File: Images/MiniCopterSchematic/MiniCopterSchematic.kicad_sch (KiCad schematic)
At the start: 21 parts, among them J1 MPU6050, M1 Motor_DC_1, M2 Motor_DC_2, M3 Motor_DC_3, M4 Motor_DC_4, Q1 FQP20NO6L, Q2 FQP20NO6L, Q3 FQP20NO6L, Q4 FQP20NO6L

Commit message: Working on PCB
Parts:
- added C1: 47UF-CAPACITOR, Capacitor_THT:CP_Radial_D4.0mm_P1.50mm, symbol SparkFun-Capacitors:47UF-POLAR-EIA3528-10V-10%
- added JP1: SolderJumper_1, Connector_PinSocket_2.54mm:PinSocket_1x02_P2.54mm_Vertical, symbol Jumper:SolderJumper_2_Open
- added JP2: SolderJumper_2, Connector_PinSocket_2.54mm:PinSocket_1x02_P2.54mm_Vertical, symbol Jumper:SolderJumper_2_Open
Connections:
- net +5V: now also C1.A (+)
- net GND: now also C1.C (-), JP1.2 (B)
- net at J1.7 (AD0): now also JP1.1 (A)
- net at J1.8 (INT): now also JP2.1 (A)
- net INT: now reaches A1.5 (D2)
- net INT: now also JP2.2 (B)
- no-connect marks 20 -> 17
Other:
- moved on the sheet: J1

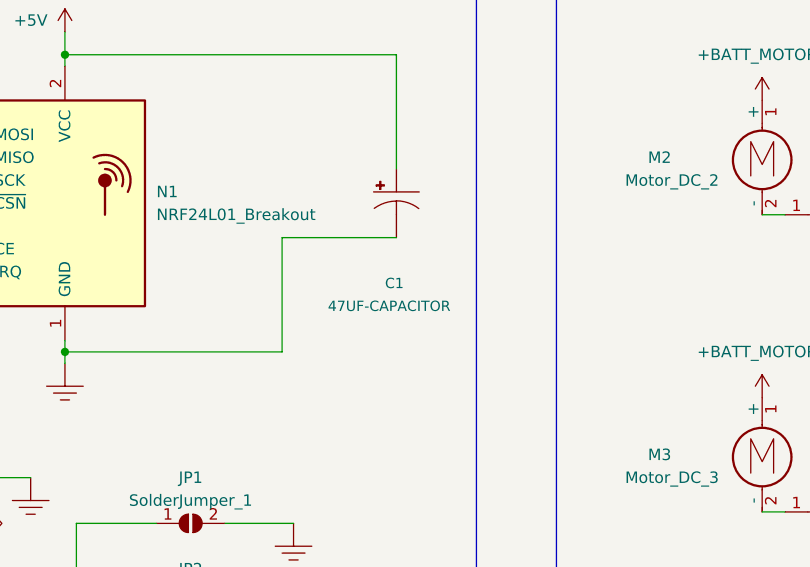
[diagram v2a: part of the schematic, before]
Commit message: Added capacitor, changed track widths on PCB
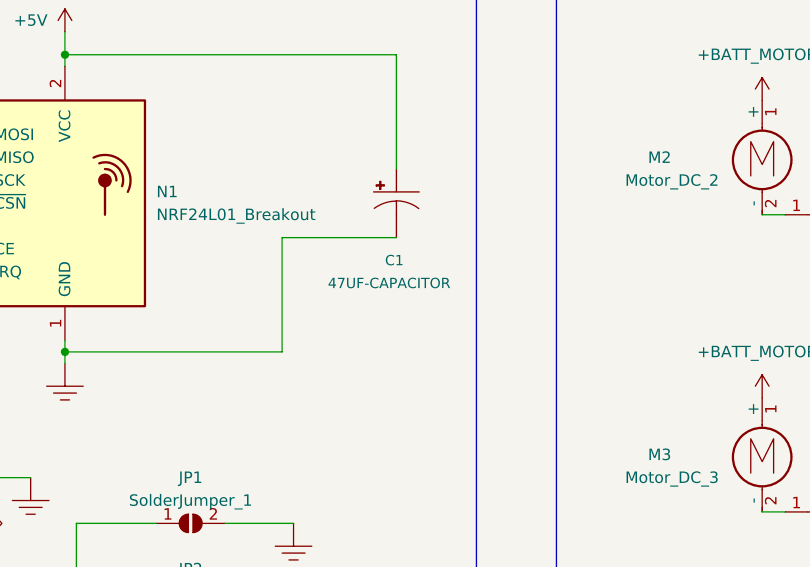
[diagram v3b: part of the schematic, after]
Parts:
- removed C1: 47UF-CAPACITOR, Capacitor_THT:CP_Radial_D4.0mm_P1.50mm, symbol SparkFun-Capacitors:47UF-POLAR-EIA3528-10V-10%
- added C1: 47UF-CAPACITOR, Capacitor_THT:CP_Radial_D6.3mm_P2.50mm, symbol AA_Custom_Components:47UF-CAPACITOR
- JP1, JP2: footprint Connector_PinSocket_2.54mm:PinSocket_1x02_P2.54mm_Vertical -> Connector_PinHeader_2.54mm:PinHeader_1x02_P2.54mm_Vertical
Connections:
- net +5V: now also C1.1 (+)
- net GND: now also C1.2 (-)

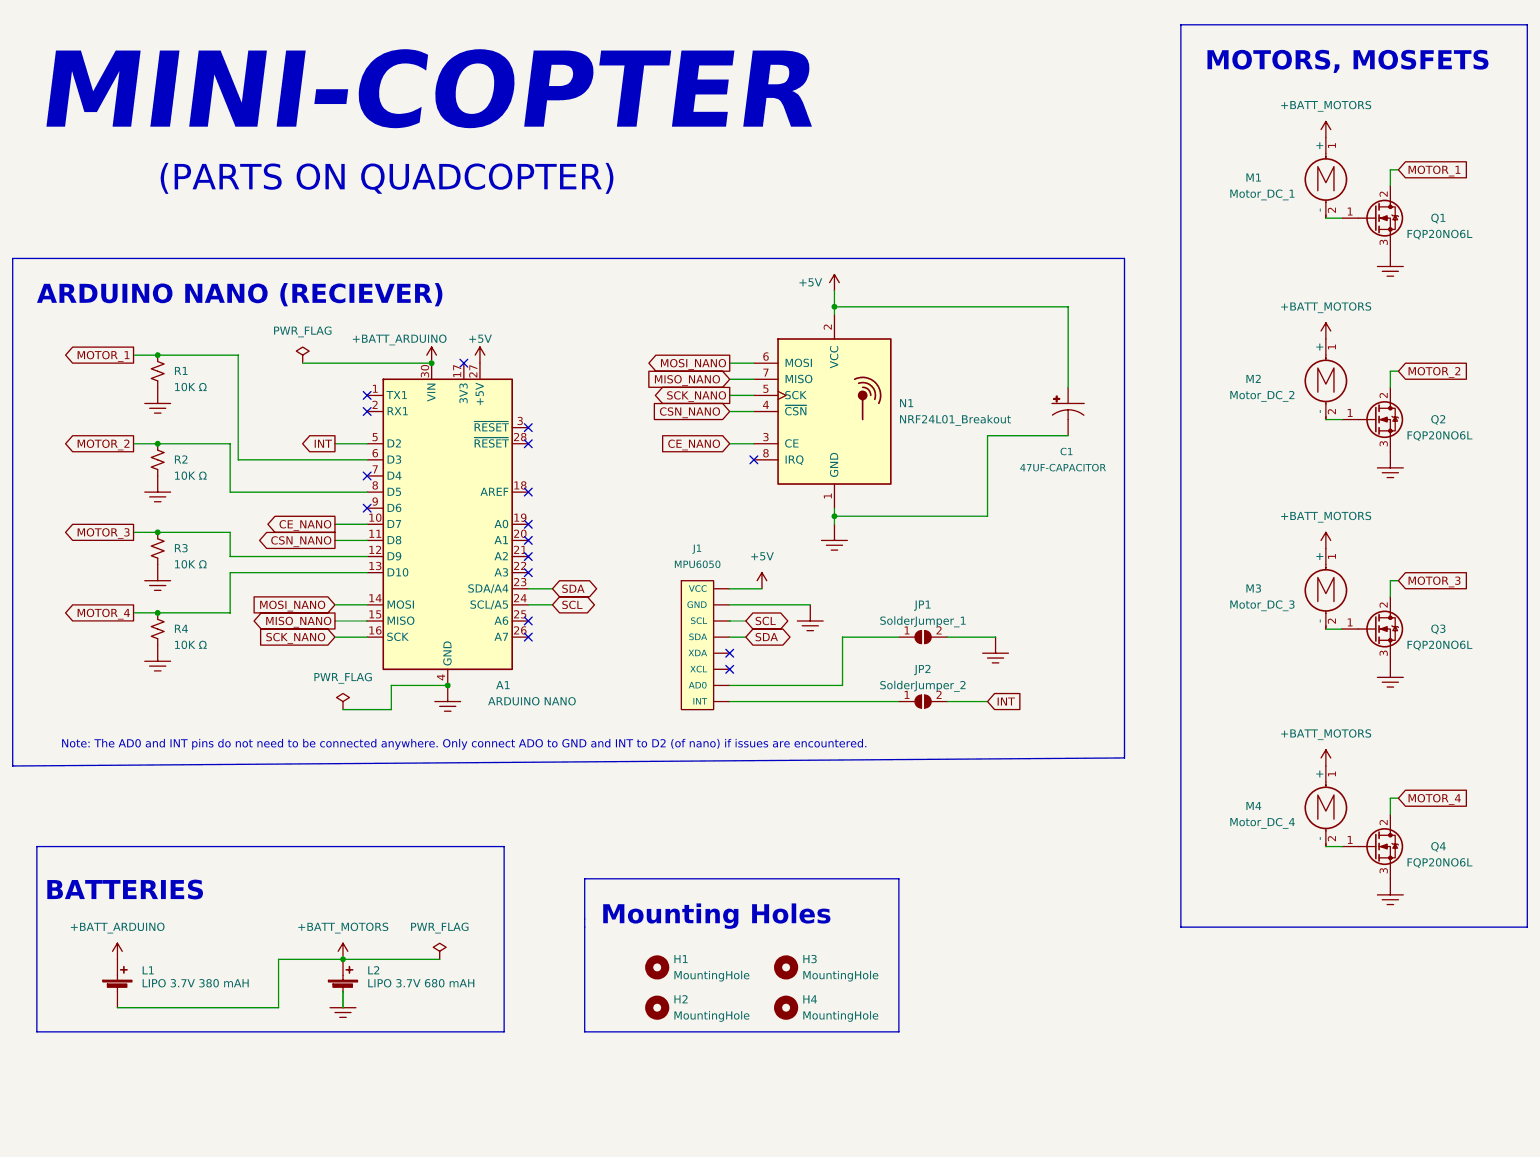
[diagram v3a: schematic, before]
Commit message: Added LEDs
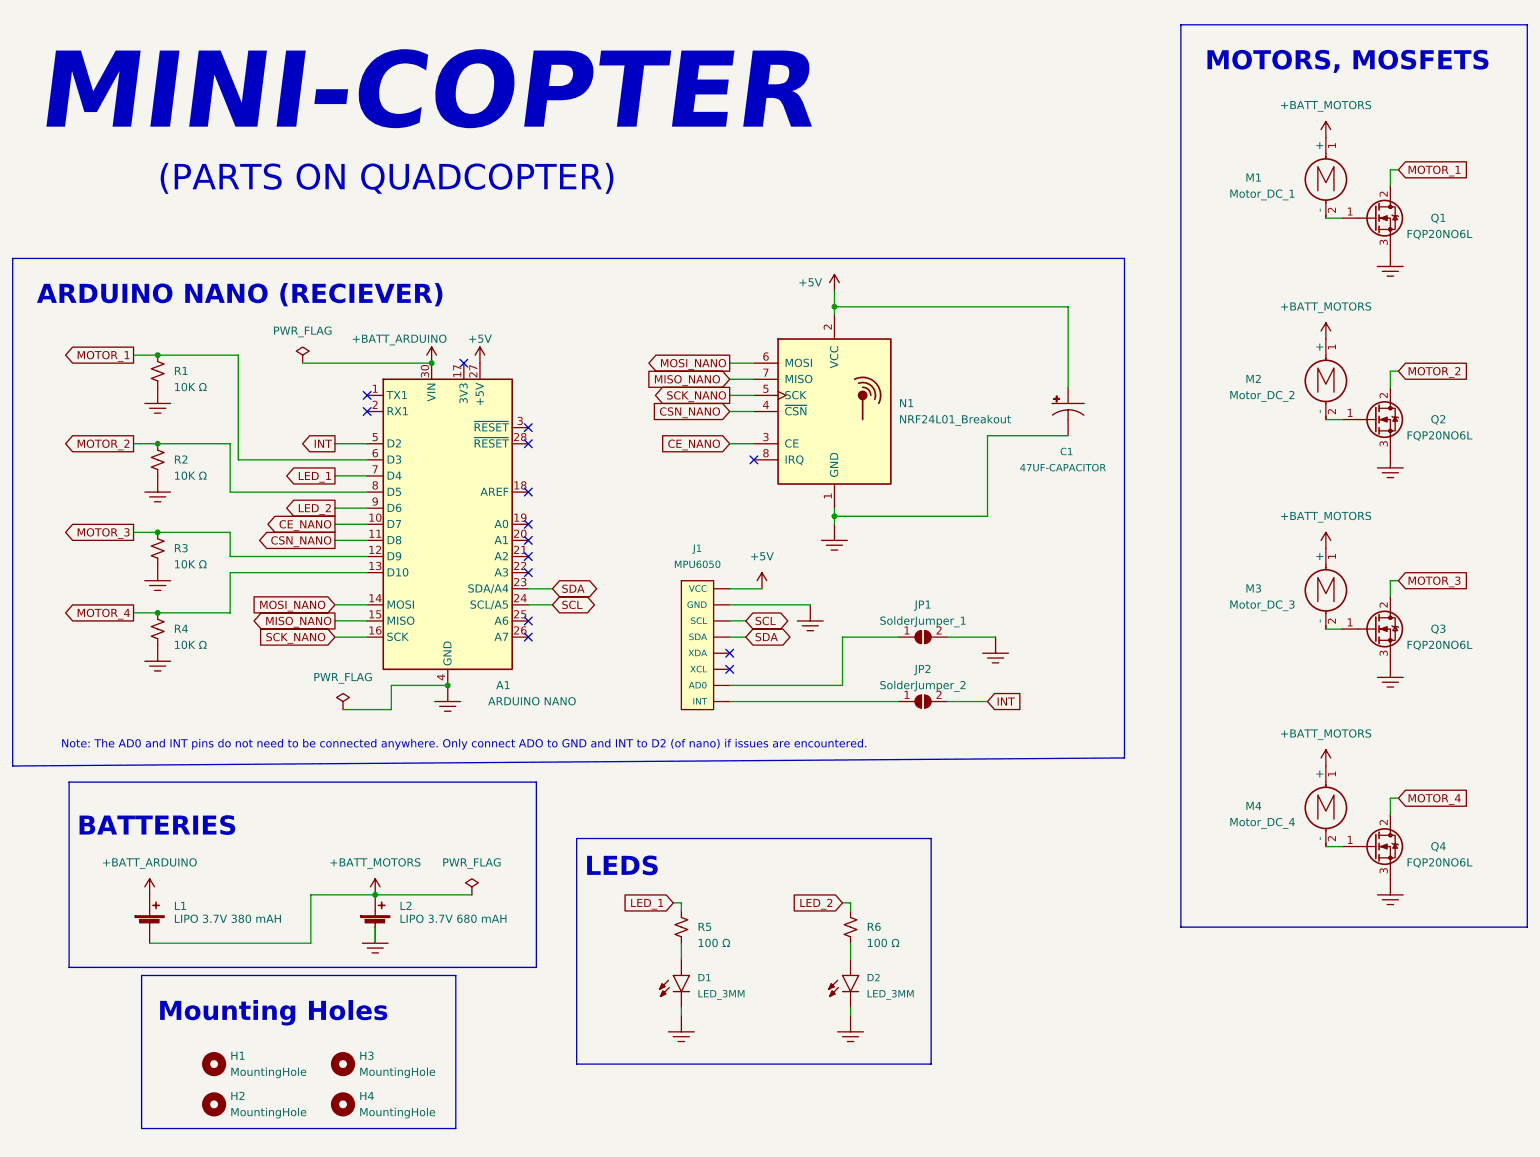
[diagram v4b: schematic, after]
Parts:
- added D1, D2: LED_3MM, LED_THT:LED_D3.0mm, symbol AA_Custom_Components:LED_3MM
- added R5, R6: 100 Ω, Resistor_THT:R_Axial_DIN0207_L6.3mm_D2.5mm_P10.16mm_Horizontal, symbol Device:R_Small_US
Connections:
- net GND: now also D1.2, D2.2
- net LED_1: now reaches A1.7 (D4)
- net LED_1: now also R5.1
- net LED_2: now reaches A1.9 (D6)
- net LED_2: now also R6.1
- new net: D1.1, R5.2
- new net: D2.1, R6.2
- no-connect marks 17 -> 15
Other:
- note added: "LEDS"
- moved on the sheet: H1, H2, H3, H4, L1, L2

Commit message: Making PCB look good
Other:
- note added: "Note: Connect JP1 to set I2C address of MPU"
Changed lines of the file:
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@@
     (effects (font (size 12 12) (thickness 1.4) bold italic) (justify left bottom))
+  )
+  (text "Note: Connect JP1 to set I2C address of MPU" (at 149.86 110.49 0)
+    (effects (font (size 1.27 1.27)) (justify left bottom))
   )
   (text "BATTERIES" (at 30.48 149.86 0)

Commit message: Updated labels
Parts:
- renumbered A1 to U1, J1 to U2, N1 to U3
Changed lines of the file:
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@@
   (symbol (lib_id "RF:NRF24L01_Breakout") (at 149.86 82.55 0) (unit 1)
     (in_bom yes) (on_board yes) (fields_autoplaced)
-    (property "Reference" "N1" (id 0) (at 160.02 81.2799 0)
+    (property "Reference" "U3" (id 0) (at 160.02 81.2799 0)
       (effects (font (size 1.27 1.27)) (justify left))
     )
@@
   (symbol (lib_name "MPU6050_IMU_1") (lib_id "AA_Custom_Components:MPU6050_IMU") (at 129.54 118.11 0) (unit 1)
     (in_bom yes) (on_board yes) (fields_autoplaced)
-    (property "Reference" "J1" (id 0) (at 128.27 104.14 0)
+    (property "Reference" "U2" (id 0) (at 128.27 104.14 0)
       (effects (font (size 1.143 1.143)))
     )
@@
   (symbol (lib_name "Arduino_Nano_Every_1") (lib_id "MCU_Module:Arduino_Nano_Every") (at 88.9 100.33 0) (unit 1)
     (in_bom yes) (on_board yes)
-    (property "Reference" "A1" (id 0) (at 96.52 125.73 0)
+    (property "Reference" "U1" (id 0) (at 96.52 125.73 0)
       (effects (font (size 1.27 1.27)) (justify left))
     )
@@
       (reference "#PWR010") (unit 1) (value "+BATT_MOTORS") (footprint "")
     )
-    (path "/edd159c8-ec25-477b-95de-4da83d07fe0d"
-      (reference "A1") (unit 1) (value "ARDUINO NANO") (footprint "AA_Custom_Components:Arduino_Nano")
-    )
     (path "/524905b1-bfdd-4409-9708-e8d25f445608"
       (reference "C1") (unit 1) (value "47UF-CAPACITOR") (footprint "Capacitor_THT:CP_Radial_D6.3mm_P2.50mm")
@@
       (reference "H4") (unit 1) (value "MountingHole") (footprint "MountingHole:MountingHole_3.2mm_M3_Pad")
     )
-    (path "/7cf07a00-d5ac-4c90-a3e7-3df1754b3724"
-      (reference "J1") (unit 1) (value "MPU6050") (footprint "AA_Custom_Components:MPU6050")
-    )
     (path "/297b4f3b-c98c-43b4-850a-e273375d03e8"
       (reference "JP1") (unit 1) (value "SolderJumper_1") (footprint "Connector_PinHeader_2.54mm:PinHeader_1x02_P2.54mm_Vertical")
@@
       (reference "M4") (unit 1) (value "Motor_DC_4") (footprint "AA_Custom_Components:PowerPad_Pair_3.0x3.0mm")
     )
-    (path "/552c74fa-1e18-46c0-a1b0-07a3fd1d445f"
-      (reference "N1") (unit 1) (value "NRF24L01_Breakout") (footprint "AA_Custom_Components:NRF24L01_Breakout")
-    )
     (path "/075952fe-8e15-4d5e-bc3f-1b285719d921"
       (reference "Q1") (unit 1) (value "FQP20NO6L") (footprint "AA_Custom_Components:3Pin_MOSFET_MotorDriver")
@@
       (reference "R6") (unit 1) (value "100 Ω") (footprint "Resistor_THT:R_Axial_DIN0207_L6.3mm_D2.5mm_P10.16mm_Horizontal")
     )
-  )
+    (path "/edd159c8-ec25-477b-95de-4da83d07fe0d"
+      (reference "U1") (unit 1) (value "ARDUINO NANO") (footprint "AA_Custom_Components:Arduino_Nano")
+    )
+    (path "/7cf07a00-d5ac-4c90-a3e7-3df1754b3724"
+      (reference "U2") (unit 1) (value "MPU6050") (footprint "AA_Custom_Components:MPU6050")
+    )
+    (path "/552c74fa-1e18-46c0-a1b0-07a3fd1d445f"
+      (reference "U3") (unit 1) (value "NRF24L01_Breakout") (footprint "AA_Custom_Components:NRF24L01_Breakout")
+    )
+  )

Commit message: PCB design finalizing
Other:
- note added: "Note: Connect JP1 to set I2C address of MPU if needed. Connect JP2 to connect Interrupt pin of MPU to D2 of Arduino if needed."
- note removed: "Note: Connect JP1 to set I2C address of MPU"
- note removed: "Note: The AD0 and INT pins do not need to be connected anywhere. Only connect ADO to GND and INT to D2 (of nano) if issues are encountered."
- moved on the sheet: C1, D1, D2, H1, H2, H3, H4, JP1, JP2, L1, L2, R1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

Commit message: Finalized PCB
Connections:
- net MOTOR_1: now also Q1.1 (G); no longer Q1.2 (D)
- net MOTOR_2: now also Q2.1 (G); no longer Q2.2 (D)
- net MOTOR_3: now also Q3.1 (G); no longer Q3.2 (D)
- net MOTOR_4: now also Q4.1 (G); no longer Q4.2 (D)
- net at M1.2 (-): now also Q1.2 (D); no longer Q1.1 (G)
- net at M3.2 (-): now also Q3.2 (D); no longer Q3.1 (G)
- net at M4.2 (-): now also Q4.2 (D); no longer Q4.1 (G)
- net at M2.2 (-): now also Q2.2 (D); no longer Q2.1 (G)
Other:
- note removed: "(PARTS ON QUADCOPTER)"
- moved on the sheet: M1, M2, M3, M4, Q1
